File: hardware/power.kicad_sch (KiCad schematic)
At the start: 11 parts, among them U30 TLV1117LV33, U31 TLV1117LV33

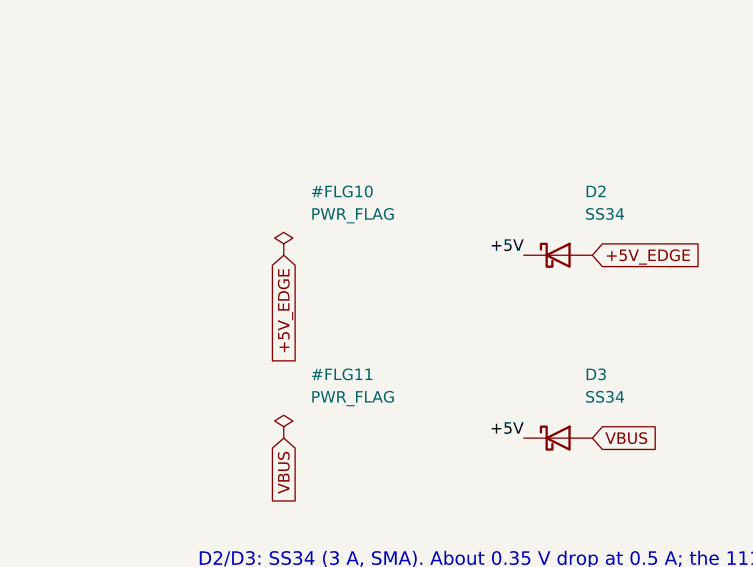
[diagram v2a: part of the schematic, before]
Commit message: Layout: netlist-driven placement of all footprints, GND/+3V3 planes
- scripts/gen_layout.py (pcbnew API): footprints from the netlist, nets,
  placement table, zones; DRC clean except unrouted connections
- connector orientations verified in the 3D render

Co-Authored-By: Claude Fable 5.1 <noreply@anthropic.com>
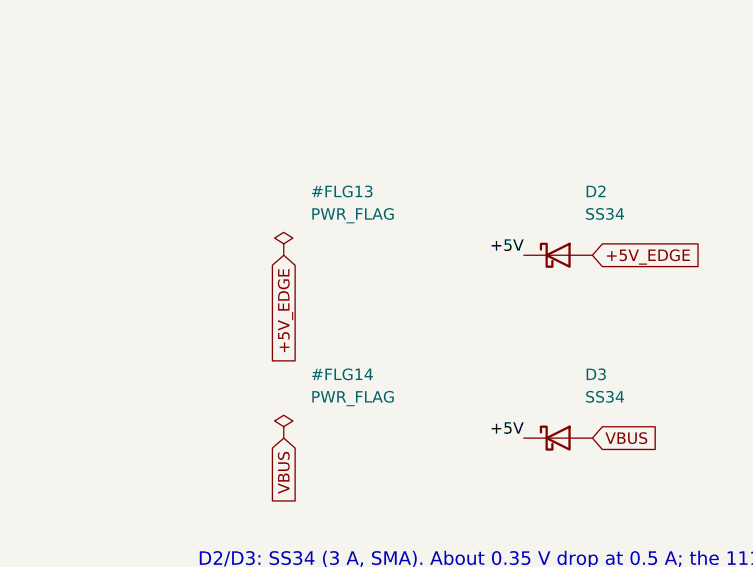
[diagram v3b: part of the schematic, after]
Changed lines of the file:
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@@
   (symbol (lib_id "power:PWR_FLAG") (at 49.53 90.17 0) (unit 1)
     (exclude_from_sim no) (in_bom yes) (on_board yes) (dnp no)
-    (property "Reference" "#FLG10" (at 52.53 83.13 0) (effects (font (size 1.27 1.27)) (justify left)))
+    (property "Reference" "#FLG13" (at 52.53 83.13 0) (effects (font (size 1.27 1.27)) (justify left)))
     (property "Value" "PWR_FLAG" (at 52.53 85.63 0) (effects (font (size 1.27 1.27)) (justify left)))
     (property "Footprint" "" (at 49.53 90.17 0) (effects (font (size 1.27 1.27)) (justify left) (hide yes)))
@@
     (property "Description" "" (at 49.53 90.17 0) (effects (font (size 1.27 1.27)) (justify left) (hide yes)))
     (pin "1")
-    (instances (project "tspico-v3" (path "/9088d141-8624-4d5c-91a9-7a3a7a90b3cc/b253c189-ca74-4c2e-8dd5-a19359172359" (reference "#FLG10") (unit 1))))
+    (instances (project "tspico-v3" (path "/9088d141-8624-4d5c-91a9-7a3a7a90b3cc/b253c189-ca74-4c2e-8dd5-a19359172359" (reference "#FLG13") (unit 1))))
   )
   (global_label "+5V_EDGE" (shape input) (at 49.53 90.17 270) (effects (font (size 1.27 1.27)) (justify right)))
   (symbol (lib_id "power:PWR_FLAG") (at 49.53 110.49 0) (unit 1)
     (exclude_from_sim no) (in_bom yes) (on_board yes) (dnp no)
-    (property "Reference" "#FLG11" (at 52.53 103.45 0) (effects (font (size 1.27 1.27)) (justify left)))
+    (property "Reference" "#FLG14" (at 52.53 103.45 0) (effects (font (size 1.27 1.27)) (justify left)))
     (property "Value" "PWR_FLAG" (at 52.53 105.95 0) (effects (font (size 1.27 1.27)) (justify left)))
     (property "Footprint" "" (at 49.53 110.49 0) (effects (font (size 1.27 1.27)) (justify left) (hide yes)))
@@
     (property "Description" "" (at 49.53 110.49 0) (effects (font (size 1.27 1.27)) (justify left) (hide yes)))
     (pin "1")
-    (instances (project "tspico-v3" (path "/9088d141-8624-4d5c-91a9-7a3a7a90b3cc/b253c189-ca74-4c2e-8dd5-a19359172359" (reference "#FLG11") (unit 1))))
+    (instances (project "tspico-v3" (path "/9088d141-8624-4d5c-91a9-7a3a7a90b3cc/b253c189-ca74-4c2e-8dd5-a19359172359" (reference "#FLG14") (unit 1))))
   )
   (global_label "VBUS" (shape input) (at 49.53 110.49 270) (effects (font (size 1.27 1.27)) (justify right)))

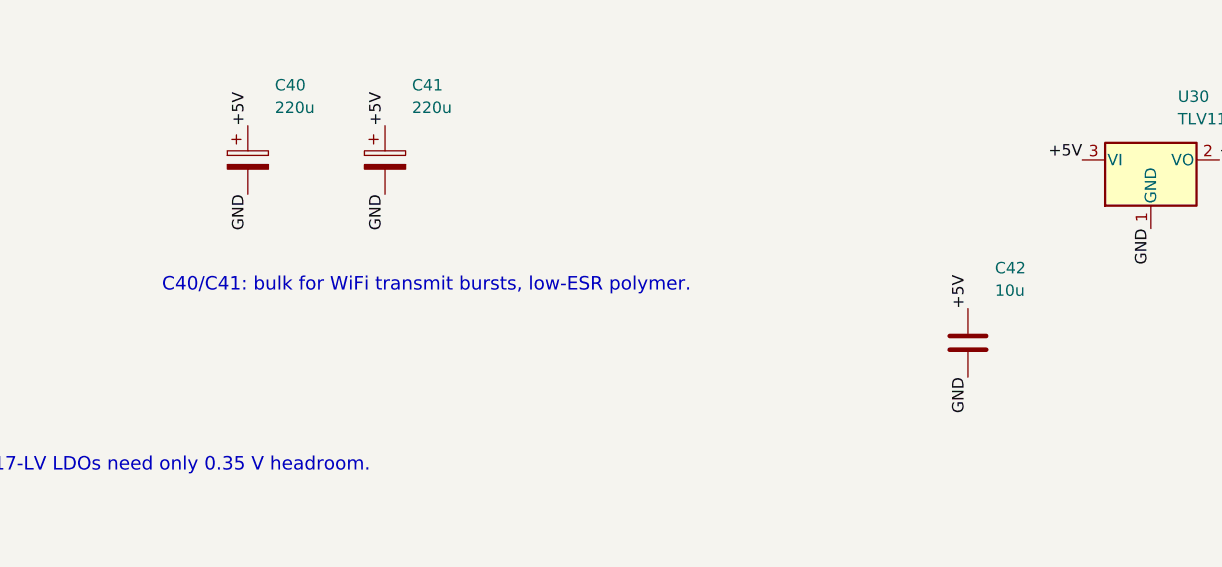
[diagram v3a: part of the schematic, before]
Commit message: BOM cost optimisation against the JLCPCB catalog; schematic-side regulator fix
jlc_price.py prices the BOM via JLCPCB's parts API. Substitutions cut parts+fees
per board from $32.95 to $17.19 on a 10-board run: PSRAM DNP, electrolytic bulk
caps, TF-01A socket, PJ-320D jack, 74HC574, GD25Q128E, 0603 10 uF, basic LED,
preferred MCP6002; U16 decoder deleted (strobes on GPIO), U8 and U15 become
74LVC245s; J3/J5 hand-soldered. Adds the AOTA inductor and VREG_AVDD filter.
PCB needs a relayout; fab/ is stale.

Co-Authored-By: Claude Fable 5.1 <noreply@anthropic.com>
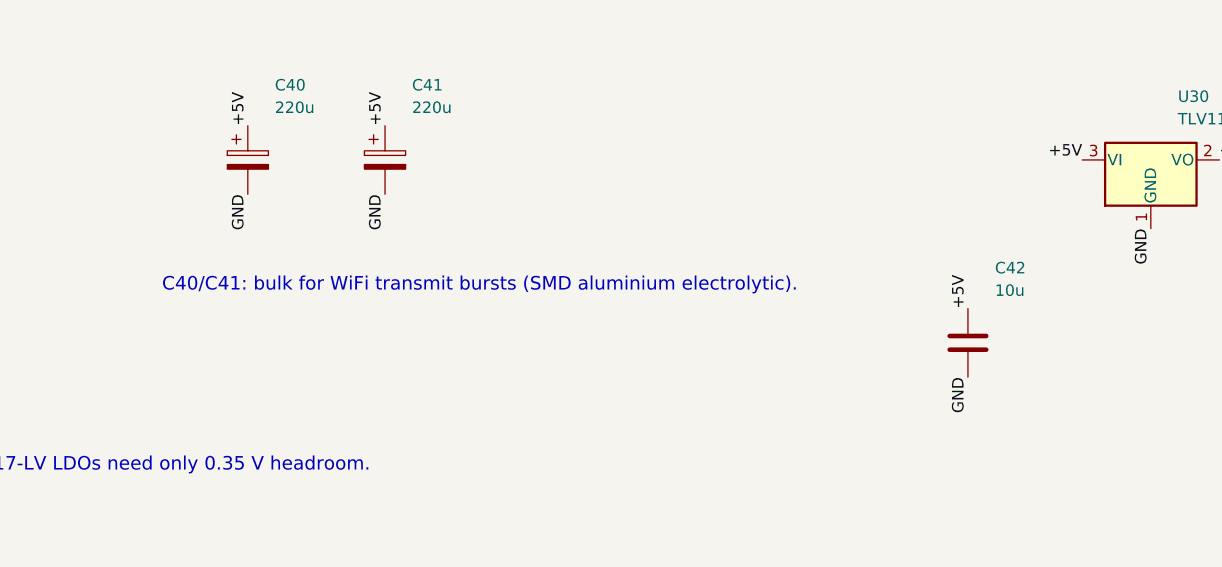
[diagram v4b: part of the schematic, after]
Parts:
- C40, C41, C46: footprint Capacitor_SMD:CP_Elec_6.3x5.9 -> Capacitor_SMD:CP_Elec_6.3x5.4; LCSC C128504 -> C2833309; MPN 6SVPC220MV -> RVT220UF10V67RV0037
- C42, C43, C44, C45: footprint Capacitor_SMD:C_0805_2012Metric -> Capacitor_SMD:C_0603_1608Metric; LCSC C15850 -> C19702; MPN CL21A106KAYNNNE -> CL10A106KP8NNNC
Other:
- note added: "C40/C41: bulk for WiFi transmit bursts (SMD aluminium electrolytic)."
- note removed: "C40/C41: bulk for WiFi transmit bursts, low-ESR polymer."
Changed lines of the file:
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@@
     (property "Reference" "C40" (at 132.54 81.86 0) (effects (font (size 1.27 1.27)) (justify left)))
     (property "Value" "220u" (at 132.54 84.36 0) (effects (font (size 1.27 1.27)) (justify left)))
-    (property "Footprint" "Capacitor_SMD:CP_Elec_6.3x5.9" (at 129.54 90.17 0) (effects (font (size 1.27 1.27)) (justify left) (hide yes)))
+    (property "Footprint" "Capacitor_SMD:CP_Elec_6.3x5.4" (at 129.54 90.17 0) (effects (font (size 1.27 1.27)) (justify left) (hide yes)))
     (property "Datasheet" "" (at 129.54 90.17 0) (effects (font (size 1.27 1.27)) (justify left) (hide yes)))
     (property "Description" "" (at 129.54 90.17 0) (effects (font (size 1.27 1.27)) (justify left) (hide yes)))
-    (property "MPN" "6SVPC220MV" (at 129.54 90.17 0) (effects (font (size 1.27 1.27)) (justify left) (hide yes)))
-    (property "LCSC" "C128504" (at 129.54 90.17 0) (effects (font (size 1.27 1.27)) (justify left) (hide yes)))
+    (property "MPN" "RVT220UF10V67RV0037" (at 129.54 90.17 0) (effects (font (size 1.27 1.27)) (justify left) (hide yes)))
+    (property "LCSC" "C2833309" (at 129.54 90.17 0) (effects (font (size 1.27 1.27)) (justify left) (hide yes)))
     (pin "1")
     (pin "2")
@@
     (property "Reference" "C41" (at 147.78 81.86 0) (effects (font (size 1.27 1.27)) (justify left)))
     (property "Value" "220u" (at 147.78 84.36 0) (effects (font (size 1.27 1.27)) (justify left)))
-    (property "Footprint" "Capacitor_SMD:CP_Elec_6.3x5.9" (at 144.78 90.17 0) (effects (font (size 1.27 1.27)) (justify left) (hide yes)))
+    (property "Footprint" "Capacitor_SMD:CP_Elec_6.3x5.4" (at 144.78 90.17 0) (effects (font (size 1.27 1.27)) (justify left) (hide yes)))
     (property "Datasheet" "" (at 144.78 90.17 0) (effects (font (size 1.27 1.27)) (justify left) (hide yes)))
     (property "Description" "" (at 144.78 90.17 0) (effects (font (size 1.27 1.27)) (justify left) (hide yes)))
-    (property "MPN" "6SVPC220MV" (at 144.78 90.17 0) (effects (font (size 1.27 1.27)) (justify left) (hide yes)))
-    (property "LCSC" "C128504" (at 144.78 90.17 0) (effects (font (size 1.27 1.27)) (justify left) (hide yes)))
+    (property "MPN" "RVT220UF10V67RV0037" (at 144.78 90.17 0) (effects (font (size 1.27 1.27)) (justify left) (hide yes)))
+    (property "LCSC" "C2833309" (at 144.78 90.17 0) (effects (font (size 1.27 1.27)) (justify left) (hide yes)))
     (pin "1")
     (pin "2")
@@
   (label "+5V" (at 144.78 86.36 90) (effects (font (size 1.27 1.27)) (justify left bottom)))
   (label "GND" (at 144.78 93.98 270) (effects (font (size 1.27 1.27)) (justify right bottom)))
-  (text "C40/C41: bulk for WiFi transmit bursts, low-ESR polymer." (exclude_from_sim no) (at 120 105 0) (effects (font (size 1.5 1.5)) (justify left bottom)))
+  (text "C40/C41: bulk for WiFi transmit bursts (SMD aluminium electrolytic)." (exclude_from_sim no) (at 120 105 0) (effects (font (size 1.5 1.5)) (justify left bottom)))
   (symbol (lib_id "Regulator_Linear:TLV1117-33") (at 229.87 90.17 0) (unit 1)
     (exclude_from_sim no) (in_bom yes) (on_board yes) (dnp no)
@@
     (property "Reference" "C42" (at 212.55 102.18 0) (effects (font (size 1.27 1.27)) (justify left)))
     (property "Value" "10u" (at 212.55 104.68 0) (effects (font (size 1.27 1.27)) (justify left)))
-    (property "Footprint" "Capacitor_SMD:C_0805_2012Metric" (at 209.55 110.49 0) (effects (font (size 1.27 1.27)) (justify left) (hide yes)))
+    (property "Footprint" "Capacitor_SMD:C_0603_1608Metric" (at 209.55 110.49 0) (effects (font (size 1.27 1.27)) (justify left) (hide yes)))
     (property "Datasheet" "" (at 209.55 110.49 0) (effects (font (size 1.27 1.27)) (justify left) (hide yes)))
     (property "Description" "" (at 209.55 110.49 0) (effects (font (size 1.27 1.27)) (justify left) (hide yes)))
-    (property "MPN" "CL21A106KAYNNNE" (at 209.55 110.49 0) (effects (font (size 1.27 1.27)) (justify left) (hide yes)))
-    (property "LCSC" "C15850" (at 209.55 110.49 0) (effects (font (size 1.27 1.27)) (justify left) (hide yes)))
+    (property "MPN" "CL10A106KP8NNNC" (at 209.55 110.49 0) (effects (font (size 1.27 1.27)) (justify left) (hide yes)))
+    (property "LCSC" "C19702" (at 209.55 110.49 0) (effects (font (size 1.27 1.27)) (justify left) (hide yes)))
     (pin "1")
     (pin "2")
@@
     (property "Reference" "C43" (at 253.19 102.18 0) (effects (font (size 1.27 1.27)) (justify left)))
     (property "Value" "10u" (at 253.19 104.68 0) (effects (font (size 1.27 1.27)) (justify left)))
-    (property "Footprint" "Capacitor_SMD:C_0805_2012Metric" (at 250.19 110.49 0) (effects (font (size 1.27 1.27)) (justify left) (hide yes)))
+    (property "Footprint" "Capacitor_SMD:C_0603_1608Metric" (at 250.19 110.49 0) (effects (font (size 1.27 1.27)) (justify left) (hide yes)))
     (property "Datasheet" "" (at 250.19 110.49 0) (effects (font (size 1.27 1.27)) (justify left) (hide yes)))
     (property "Description" "" (at 250.19 110.49 0) (effects (font (size 1.27 1.27)) (justify left) (hide yes)))
-    (property "MPN" "CL21A106KAYNNNE" (at 250.19 110.49 0) (effects (font (size 1.27 1.27)) (justify left) (hide yes)))
-    (property "LCSC" "C15850" (at 250.19 110.49 0) (effects (font (size 1.27 1.27)) (justify left) (hide yes)))
+    (property "MPN" "CL10A106KP8NNNC" (at 250.19 110.49 0) (effects (font (size 1.27 1.27)) (justify left) (hide yes)))
+    (property "LCSC" "C19702" (at 250.19 110.49 0) (effects (font (size 1.27 1.27)) (justify left) (hide yes)))
     (pin "1")
     (pin "2")
@@
     (property "Reference" "C44" (at 212.55 172.03 0) (effects (font (size 1.27 1.27)) (justify left)))
     (property "Value" "10u" (at 212.55 174.53 0) (effects (font (size 1.27 1.27)) (justify left)))
-    (property "Footprint" "Capacitor_SMD:C_0805_2012Metric" (at 209.55 180.34 0) (effects (font (size 1.27 1.27)) (justify left) (hide yes)))
+    (property "Footprint" "Capacitor_SMD:C_0603_1608Metric" (at 209.55 180.34 0) (effects (font (size 1.27 1.27)) (justify left) (hide yes)))
     (property "Datasheet" "" (at 209.55 180.34 0) (effects (font (size 1.27 1.27)) (justify left) (hide yes)))
     (property "Description" "" (at 209.55 180.34 0) (effects (font (size 1.27 1.27)) (justify left) (hide yes)))
-    (property "MPN" "CL21A106KAYNNNE" (at 209.55 180.34 0) (effects (font (size 1.27 1.27)) (justify left) (hide yes)))
-    (property "LCSC" "C15850" (at 209.55 180.34 0) (effects (font (size 1.27 1.27)) (justify left) (hide yes)))
+    (property "MPN" "CL10A106KP8NNNC" (at 209.55 180.34 0) (effects (font (size 1.27 1.27)) (justify left) (hide yes)))
+    (property "LCSC" "C19702" (at 209.55 180.34 0) (effects (font (size 1.27 1.27)) (justify left) (hide yes)))
     (pin "1")
     (pin "2")
@@
     (property "Reference" "C45" (at 243.03 172.03 0) (effects (font (size 1.27 1.27)) (justify left)))
     (property "Value" "10u" (at 243.03 174.53 0) (effects (font (size 1.27 1.27)) (justify left)))
-    (property "Footprint" "Capacitor_SMD:C_0805_2012Metric" (at 240.03 180.34 0) (effects (font (size 1.27 1.27)) (justify left) (hide yes)))
+    (property "Footprint" "Capacitor_SMD:C_0603_1608Metric" (at 240.03 180.34 0) (effects (font (size 1.27 1.27)) (justify left) (hide yes)))
     (property "Datasheet" "" (at 240.03 180.34 0) (effects (font (size 1.27 1.27)) (justify left) (hide yes)))
     (property "Description" "" (at 240.03 180.34 0) (effects (font (size 1.27 1.27)) (justify left) (hide yes)))
-    (property "MPN" "CL21A106KAYNNNE" (at 240.03 180.34 0) (effects (font (size 1.27 1.27)) (justify left) (hide yes)))
-    (property "LCSC" "C15850" (at 240.03 180.34 0) (effects (font (size 1.27 1.27)) (justify left) (hide yes)))
+    (property "MPN" "CL10A106KP8NNNC" (at 240.03 180.34 0) (effects (font (size 1.27 1.27)) (justify left) (hide yes)))
+    (property "LCSC" "C19702" (at 240.03 180.34 0) (effects (font (size 1.27 1.27)) (justify left) (hide yes)))
     (pin "1")
     (pin "2")
@@
     (property "Reference" "C46" (at 273.51 172.03 0) (effects (font (size 1.27 1.27)) (justify left)))
     (property "Value" "220u" (at 273.51 174.53 0) (effects (font (size 1.27 1.27)) (justify left)))
-    (property "Footprint" "Capacitor_SMD:CP_Elec_6.3x5.9" (at 270.51 180.34 0) (effects (font (size 1.27 1.27)) (justify left) (hide yes)))
+    (property "Footprint" "Capacitor_SMD:CP_Elec_6.3x5.4" (at 270.51 180.34 0) (effects (font (size 1.27 1.27)) (justify left) (hide yes)))
     (property "Datasheet" "" (at 270.51 180.34 0) (effects (font (size 1.27 1.27)) (justify left) (hide yes)))
     (property "Description" "" (at 270.51 180.34 0) (effects (font (size 1.27 1.27)) (justify left) (hide yes)))
-    (property "MPN" "6SVPC220MV" (at 270.51 180.34 0) (effects (font (size 1.27 1.27)) (justify left) (hide yes)))
-    (property "LCSC" "C128504" (at 270.51 180.34 0) (effects (font (size 1.27 1.27)) (justify left) (hide yes)))
+    (property "MPN" "RVT220UF10V67RV0037" (at 270.51 180.34 0) (effects (font (size 1.27 1.27)) (justify left) (hide yes)))
+    (property "LCSC" "C2833309" (at 270.51 180.34 0) (effects (font (size 1.27 1.27)) (justify left) (hide yes)))
     (pin "1")
     (pin "2")
